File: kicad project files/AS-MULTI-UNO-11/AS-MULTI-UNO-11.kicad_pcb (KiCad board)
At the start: 2 copper layers, 75.6 x 54 mm, 13 parts, among them J1 ICSP, J2 Conn_01x02, J3 Conn_01x06, SW1 SW_Push, U1 ATmega328-P, Y1 16Mhz

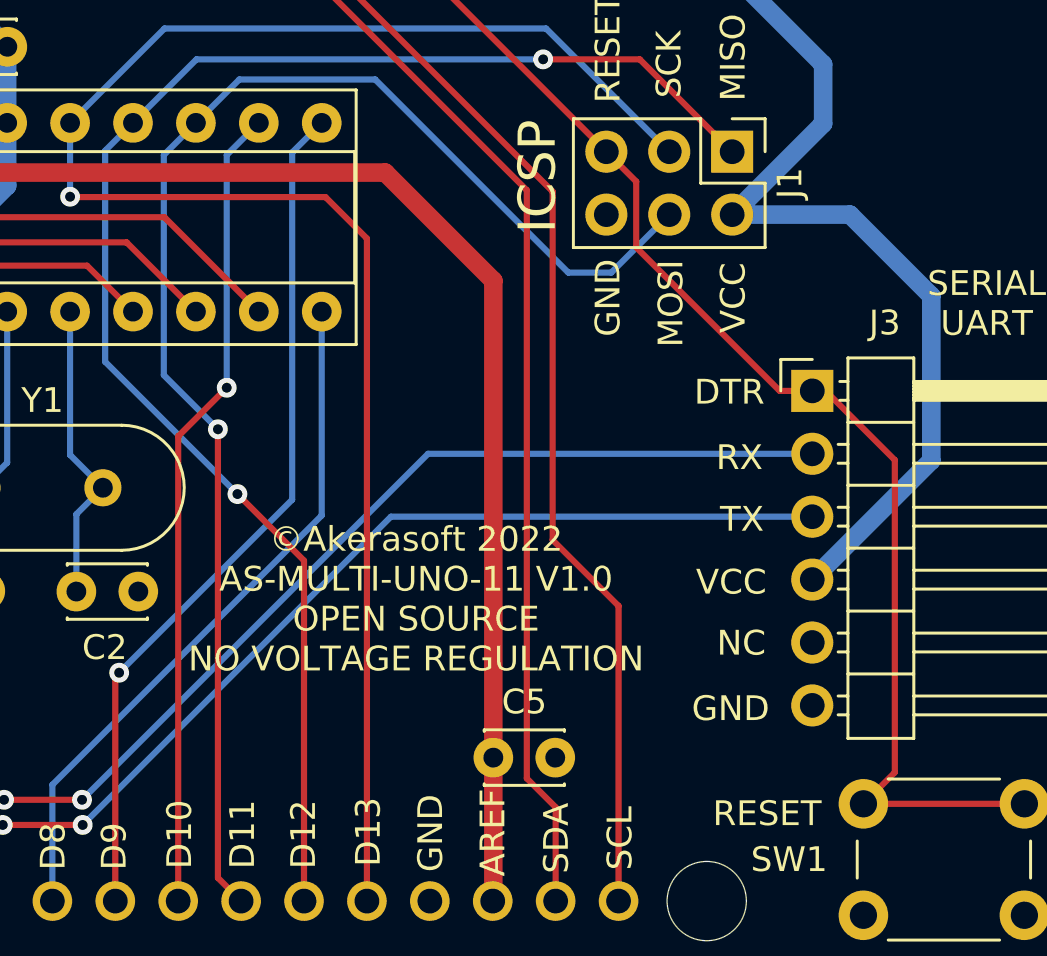
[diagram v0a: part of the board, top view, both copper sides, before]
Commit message: Fix FTDI cable connector, add capacitor, GND CTS
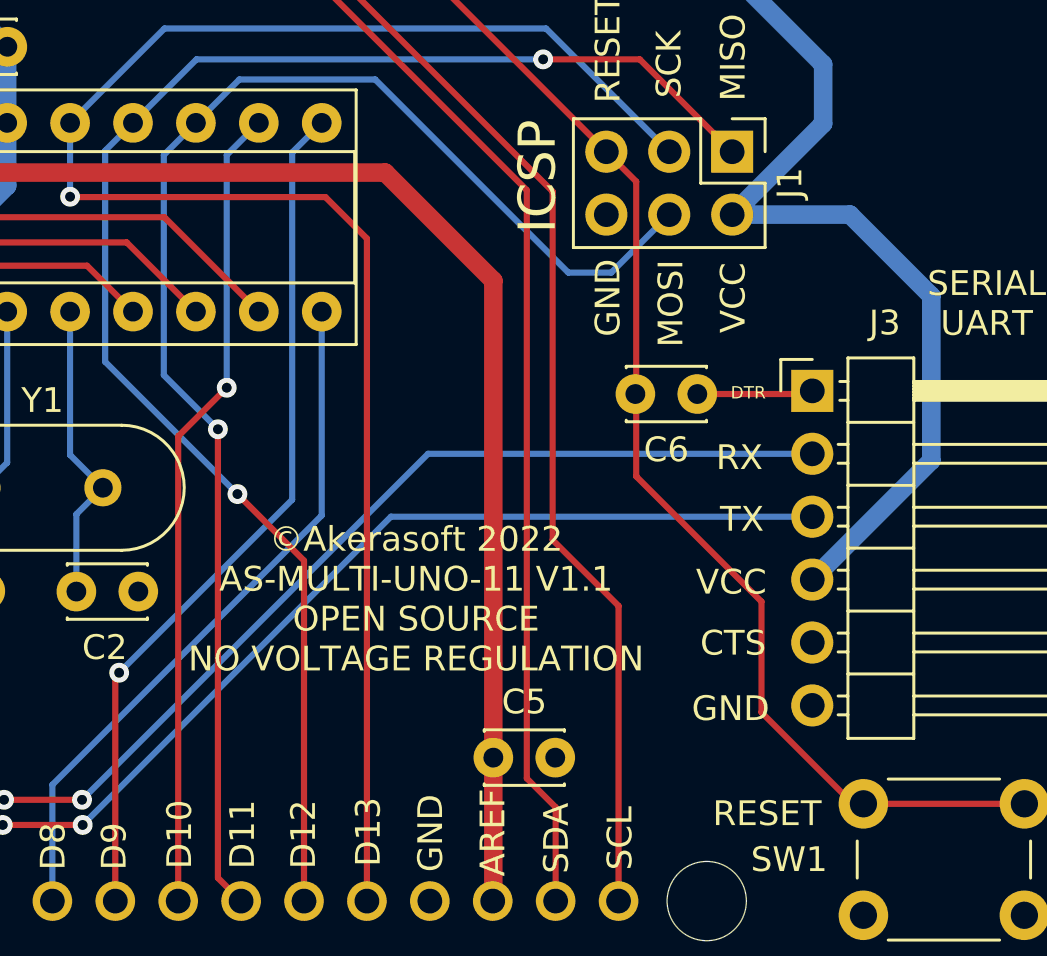
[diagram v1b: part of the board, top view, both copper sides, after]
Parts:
- added C6: 100nF, Capacitor_THT:C_Disc_D3.0mm_W2.0mm_P2.50mm, F.Cu at (130.1, 94.6)
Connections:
- A1 pad 3: /DTR -> /RESET
- J1 pad 5: /DTR -> /RESET
- J3 pad 5: /CTS -> GND
- R1 pad 2: /DTR -> /RESET
- SW1 pad 1: /DTR -> /RESET
- U1 pad 1: /DTR -> /RESET
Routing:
- net /RESET: track 0.00 -> 111.0 mm
- net /DTR: track 112.9 -> 4.69 mm
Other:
- board text added: "CTS"
- board text added: "©Akerasoft 2022 AS-MULTI-UNO-11 V1.1 OPEN SOURCE NO VOLTAGE REGULATION"
- board text removed: "©Akerasoft 2022 AS-MULTI-UNO-11 V1.0 OPEN SOURCE NO VOLTAGE REGULATION"
